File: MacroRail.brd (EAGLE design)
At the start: 42.9 x 81.5 mm, 13 parts, among them CN1 1X4-3.5MM, T1 2N2222, U1 ESP32DEVKITC, U2 TCM2209-V1.2

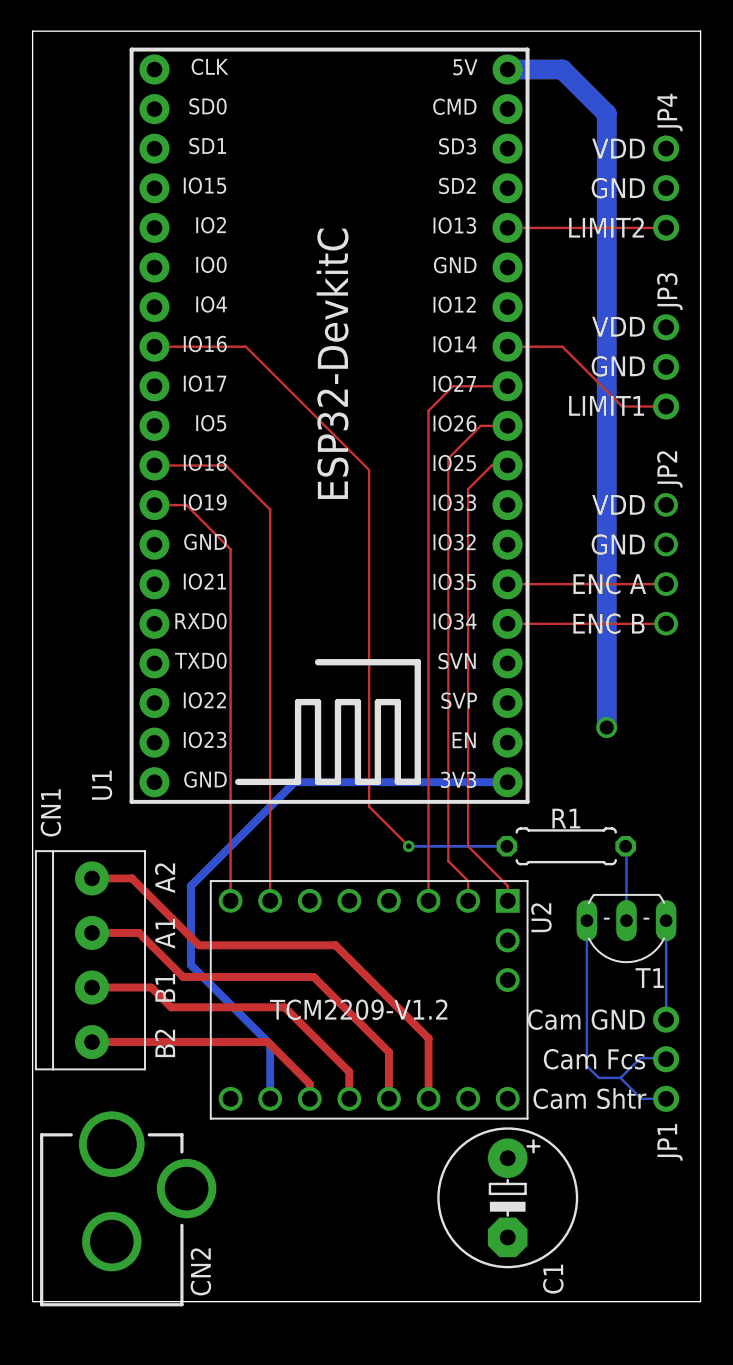
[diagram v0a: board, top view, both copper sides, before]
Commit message: Add mounting holes and better outputs
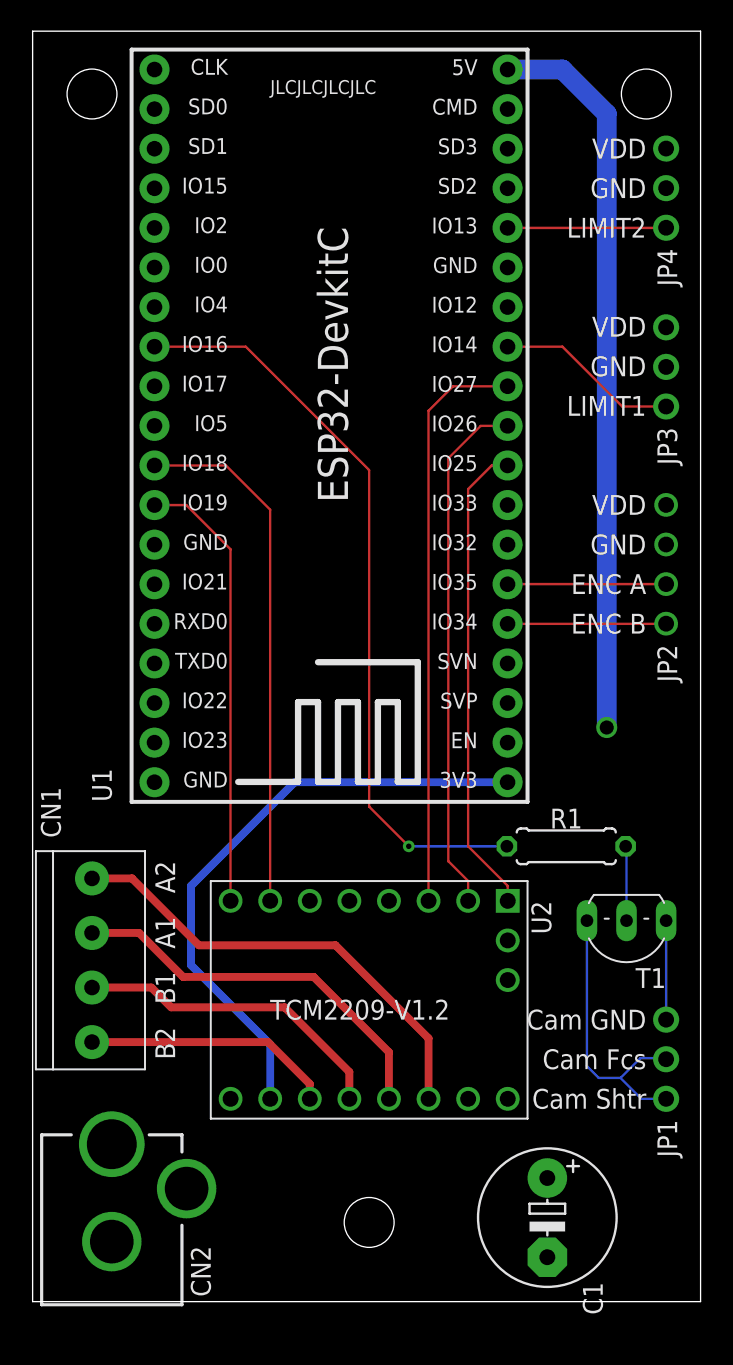
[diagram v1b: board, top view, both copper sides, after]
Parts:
- moved C1 2.84 mm to (33.0, 5.39)
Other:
- board text added: "JLCJLCJLCJLC"
- board text added: "Vin (5-12V)"

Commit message: Adding basic BOM to README
Adding Bill of Materials and links to example Aliexpress listings.
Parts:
- C1: value (none) -> 470uF
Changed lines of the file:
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@@
 <attribute name="VALUE" x="15.24" y="18.09" size="1.27" layer="27"/>
 </element>
-<element name="C1" library="rcl" library_urn="urn:adsk.eagle:library:334" package="E5-8,5" package3d_urn="urn:adsk.eagle:package:23374/1" override_package3d_urn="urn:adsk.eagle:package:34287653/3" override_package_urn="urn:adsk.eagle:footprint:22875/1" value="" x="33.02" y="5.39" smashed="yes" rot="R270">
+<element name="C1" library="rcl" library_urn="urn:adsk.eagle:library:334" package="E5-8,5" package3d_urn="urn:adsk.eagle:package:23374/1" override_package3d_urn="urn:adsk.eagle:package:34287653/3" override_package_urn="urn:adsk.eagle:footprint:22875/1" value="470uF" x="33.02" y="5.39" smashed="yes" rot="R270">
 <attribute name="NAME" x="35.306" y="1.2498" size="1.27" layer="25" ratio="10" rot="R270"/>
 <attribute name="POPULARITY" value="4" x="33.02" y="5.39" size="1.778" layer="27" rot="R270" display="off"/>

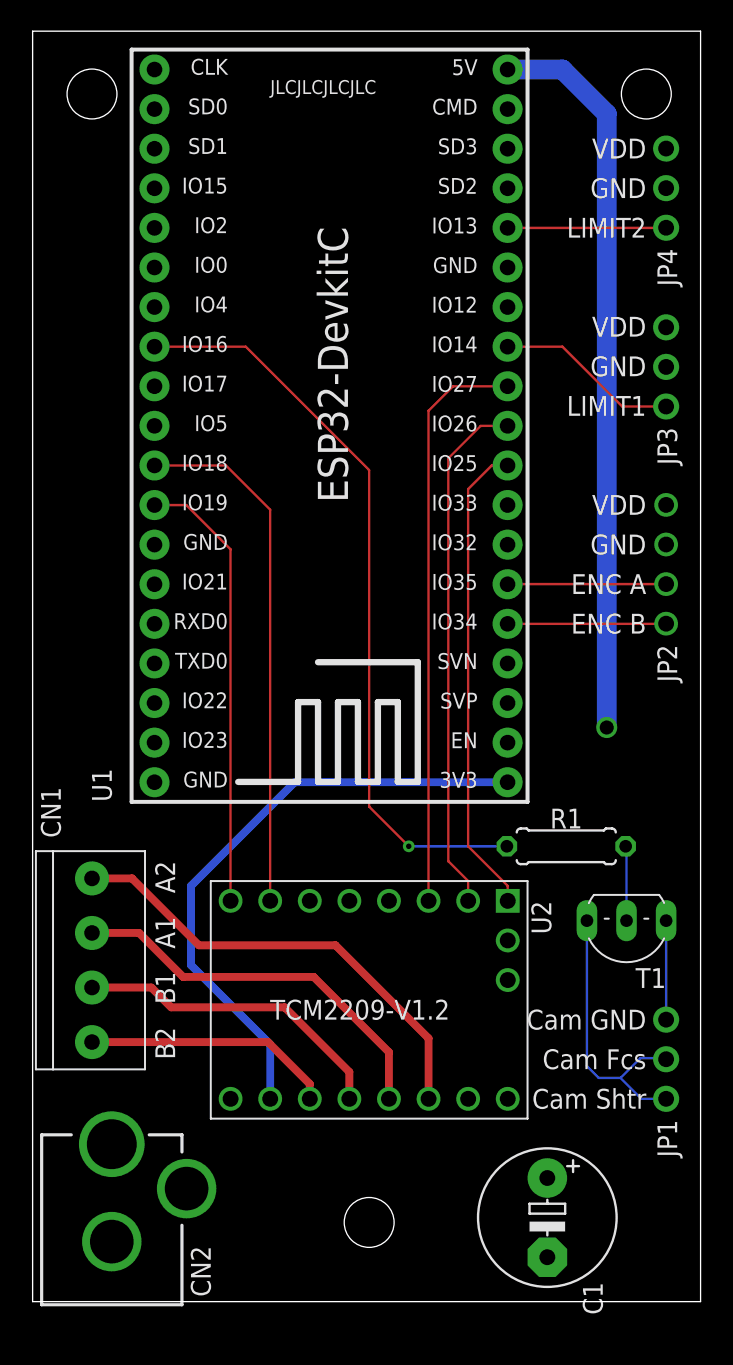
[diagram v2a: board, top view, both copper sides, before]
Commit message: Redesigned shutter circuit
Complete redesign of the shutter circuit to make it more flexible and camera agnostic. The user will have to modify the board to match with what their camera expects.
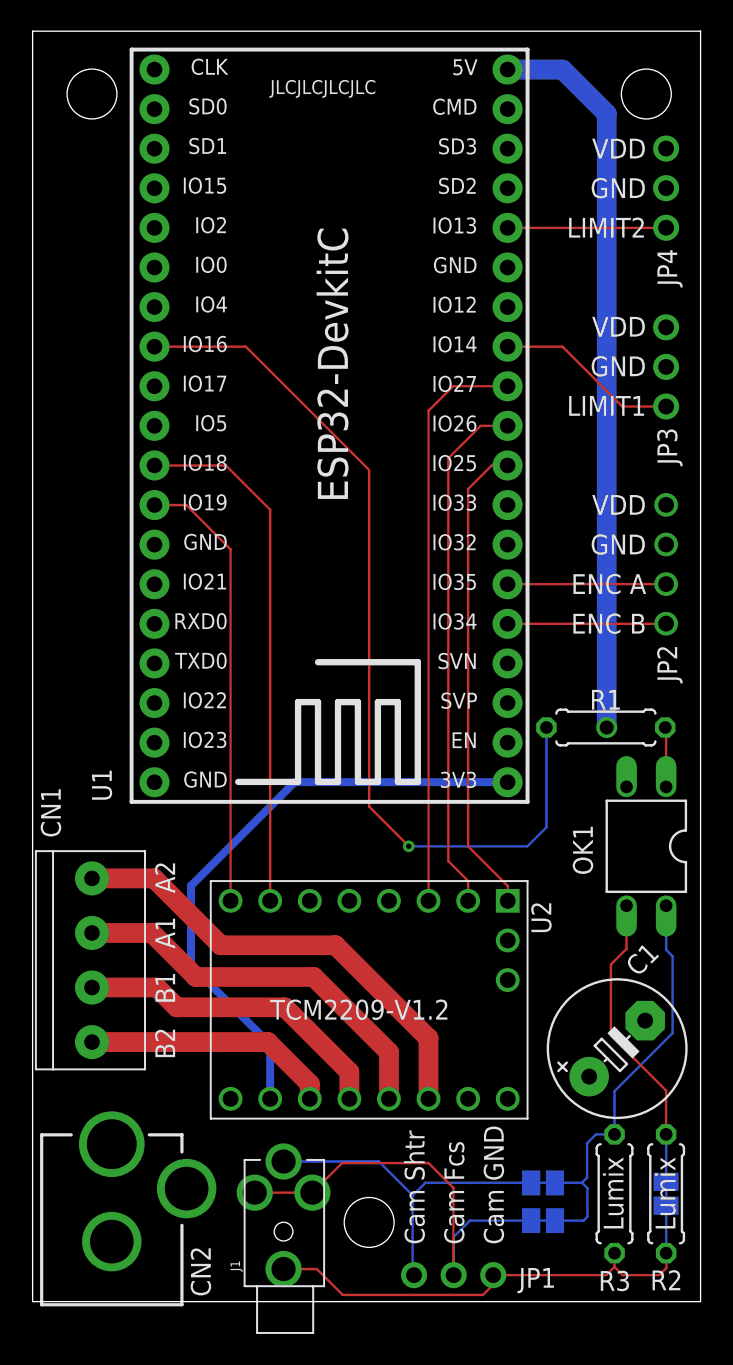
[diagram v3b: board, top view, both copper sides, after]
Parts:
- removed T1: 2N2222, adafruit:TO92-EBC-OVAL
- added J1: SJ1-2503A, 00-Random-Components-Simen:STEREOJACK2.5MM_STEREOJACK2.5MM
- added OK1: PC817, optocoupler:DIL04
- added R2: 2k, rcl:0207/7
- added R3: 46k, rcl:0207/7
- added SJ1, SJ2, SJ3: (no value), jumper:SJ
- R1: value 1k -> 600R
- moved JP1 19.4 mm to (27.0, 1.70), turned to 0 degrees
- moved C1 11.7 mm to (37.5, 16.2), turned to 45 degrees
- moved R1 8.03 mm to (36.8, 36.8)
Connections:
- removed net N$3: R1.1, T1.B
- new net N$1: OK1.1, R1.1
- net CAM_FOCUS_SHUTTER: now also J1.RING, J1.TIP1, J1.TIP2, OK1.4, R3.1, SJ2.1, SJ2.2, SJ3.1, SJ3.2; no longer T1.C
- net CAM_GND: now also J1.SHIELD, OK1.3, R2.1, R2.2, R3.2, SJ1.1, SJ1.2; no longer T1.E
- net GND: now also OK1.2
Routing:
- net CAM_FOCUS_SHUTTER: track 18.8 -> 80.3 mm
- net CAM_GND: track 6.35 -> 52.8 mm
- net SHUTTER: track 48.5 -> 58.0 mm
- net N$3: track 4.79 -> 0.00 mm
- net N$1: track 0.00 -> 3.83 mm
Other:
- board text added: "Lumix"

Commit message: V1.0
Redesigned power planes and added more documentation in silk screen.
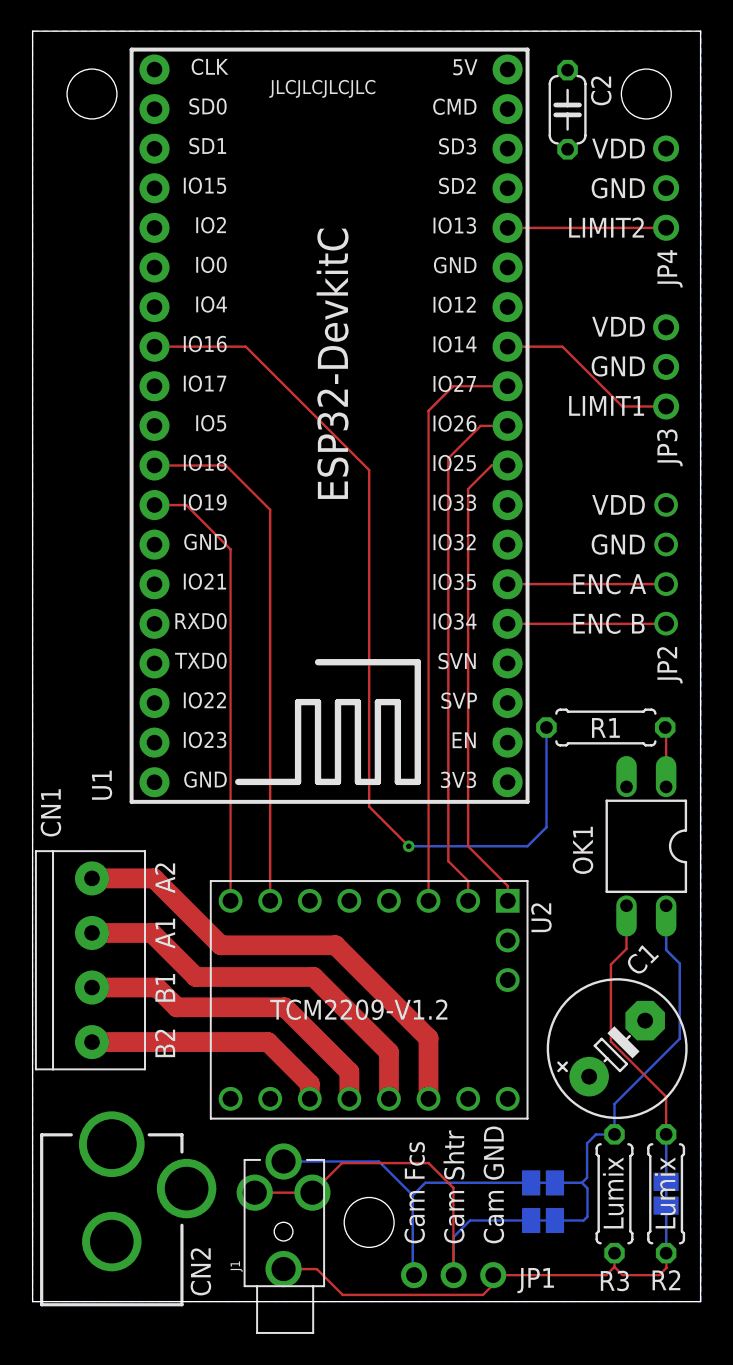
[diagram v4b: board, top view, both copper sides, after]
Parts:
- added C2: 1uF, rcl:C050-024X044
- C1: value 470uF -> 100uF
- moved U$2 2.54 mm to (21.6, 73.7)
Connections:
- net GND: now also C2.1
- net V_MOTOR: now also C2.2
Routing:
- net V_MOTOR: track 46.9 -> 0.00 mm, vias 1 -> 0
- net VDD: track 38.8 -> 0.00 mm
- added copper zone on layer 16, net V_MOTOR
- removed copper zone on layer 15, net V_MOTOR
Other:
- board text added: "Docs: GitHub.com/AppliedProcrastination"
- board text added: "Motorized Macro Slider V1.0"
- board text added: "RING"
- board text added: "TIP"
- board text added: "User must verify shutter-circuit compatibility with their camera (configurable via SJ1-3 and R2-3)"
